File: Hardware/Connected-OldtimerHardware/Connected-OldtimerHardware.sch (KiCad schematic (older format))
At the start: 16 parts, among them J1 CAN_Bus_Connector, J2 MainConnector, J3 NextionConnector, Q1 2N3906, U1 ParticleElectron, U2 TSR_2-2450, U3 CANTranceiverModule, U4 AdafruitFRAM, U5 AdafruitUltimateGPS, U6 MotionSensor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

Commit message: reordered can module pins
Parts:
- U3: footprint (none) -> heathsfootprints:CAN_Tranceiver_Module
- U4: footprint (none) -> heathsfootprints:Adafruit_I2C_FRAM
- U5: footprint (none) -> heathsfootprints:AdafruitUltimateGPS
- U6: footprint (none) -> heathsfootprints:ShockSensor
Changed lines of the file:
@@
 F 0 "U3" H 4977 1446 50  0000 L CNN
 F 1 "CANTranceiverModule" H 4977 1355 50  0000 L CNN
-F 2 "" H 4950 1300 50  0001 C CNN
+F 2 "heathsfootprints:CAN_Tranceiver_Module" H 4950 1300 50  0001 C CNN
 F 3 "" H 4950 1300 50  0001 C CNN
 	1    4950 1300
@@
 F 0 "U4" H 5078 2746 50  0000 L CNN
 F 1 "AdafruitFRAM" H 5078 2655 50  0000 L CNN
-F 2 "" H 4600 2800 50  0001 C CNN
+F 2 "heathsfootprints:Adafruit_I2C_FRAM" H 4600 2800 50  0001 C CNN
 F 3 "" H 4600 2800 50  0001 C CNN
 	1    4600 2800
@@
 F 0 "U5" H 5127 4771 50  0000 L CNN
 F 1 "AdafruitUltimateGPS" H 5127 4680 50  0000 L CNN
-F 2 "" H 4750 4700 50  0001 C CNN
+F 2 "heathsfootprints:AdafruitUltimateGPS" H 4750 4700 50  0001 C CNN
 F 3 "" H 4750 4700 50  0001 C CNN
 	1    4750 4700
@@
 F 0 "U6" H 7377 3246 50  0000 L CNN
 F 1 "MotionSensor" H 7377 3155 50  0000 L CNN
-F 2 "" H 7300 3200 50  0001 C CNN
+F 2 "heathsfootprints:ShockSensor" H 7300 3200 50  0001 C CNN
 F 3 "" H 7300 3200 50  0001 C CNN
 	1    7300 3200

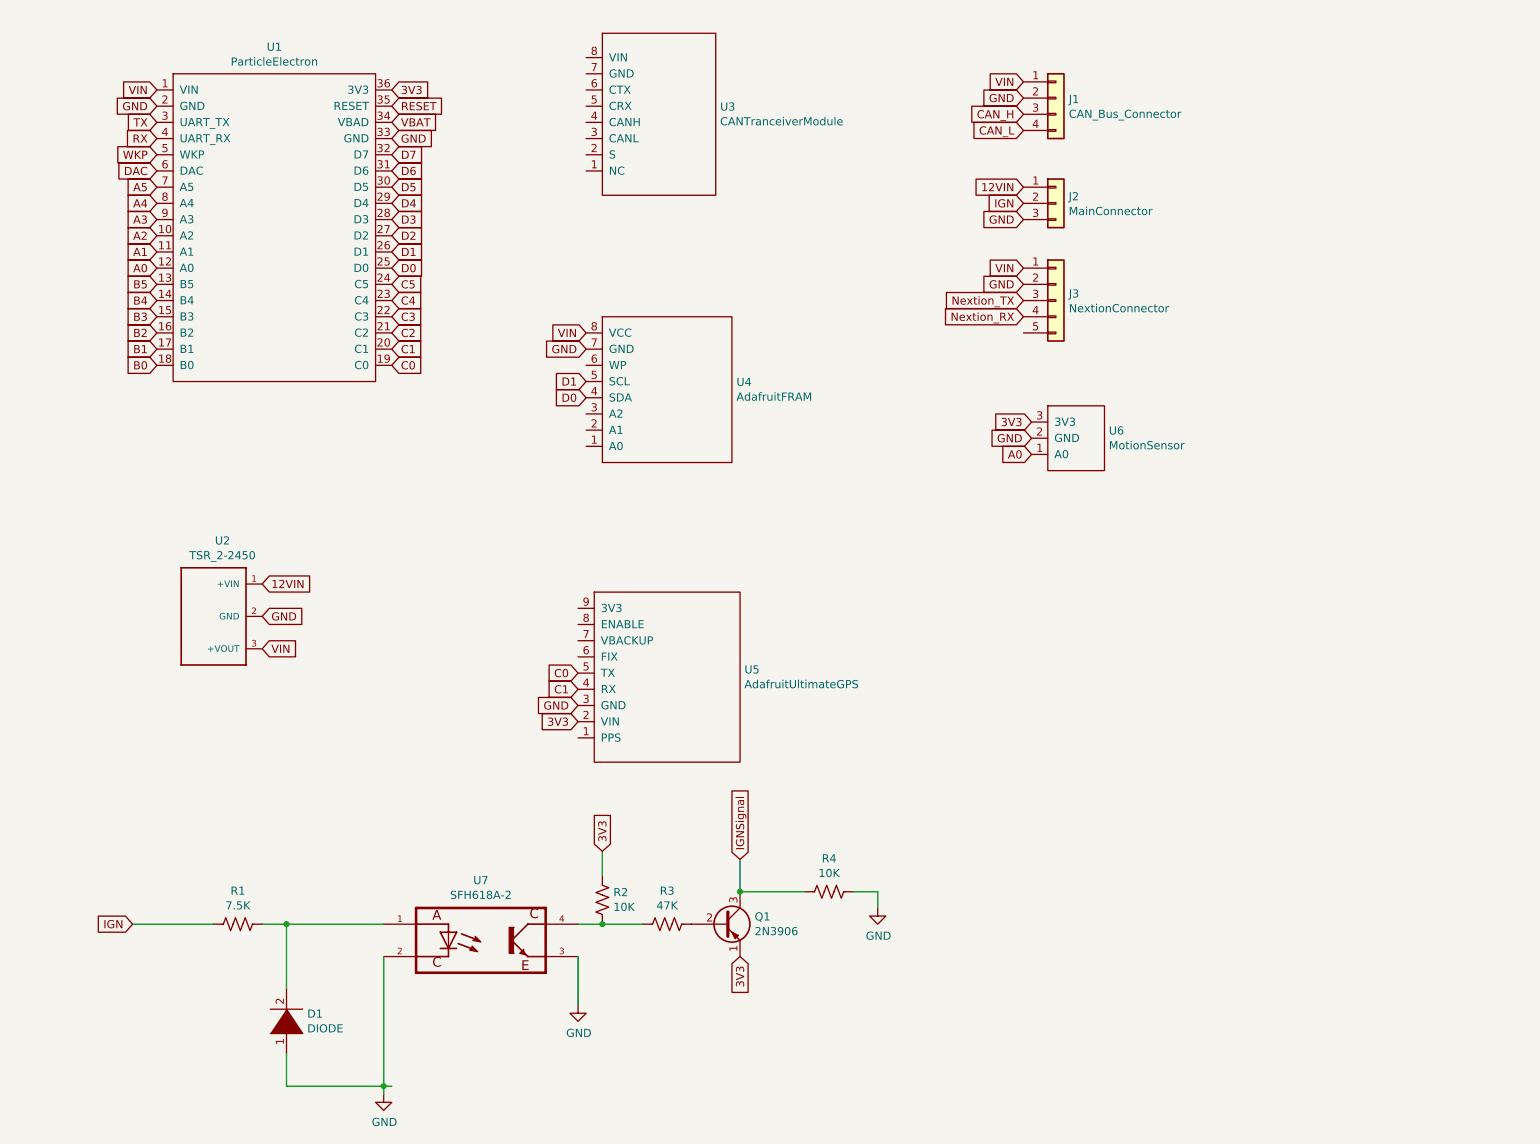
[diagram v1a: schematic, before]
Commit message: renamed pinflags to purposes
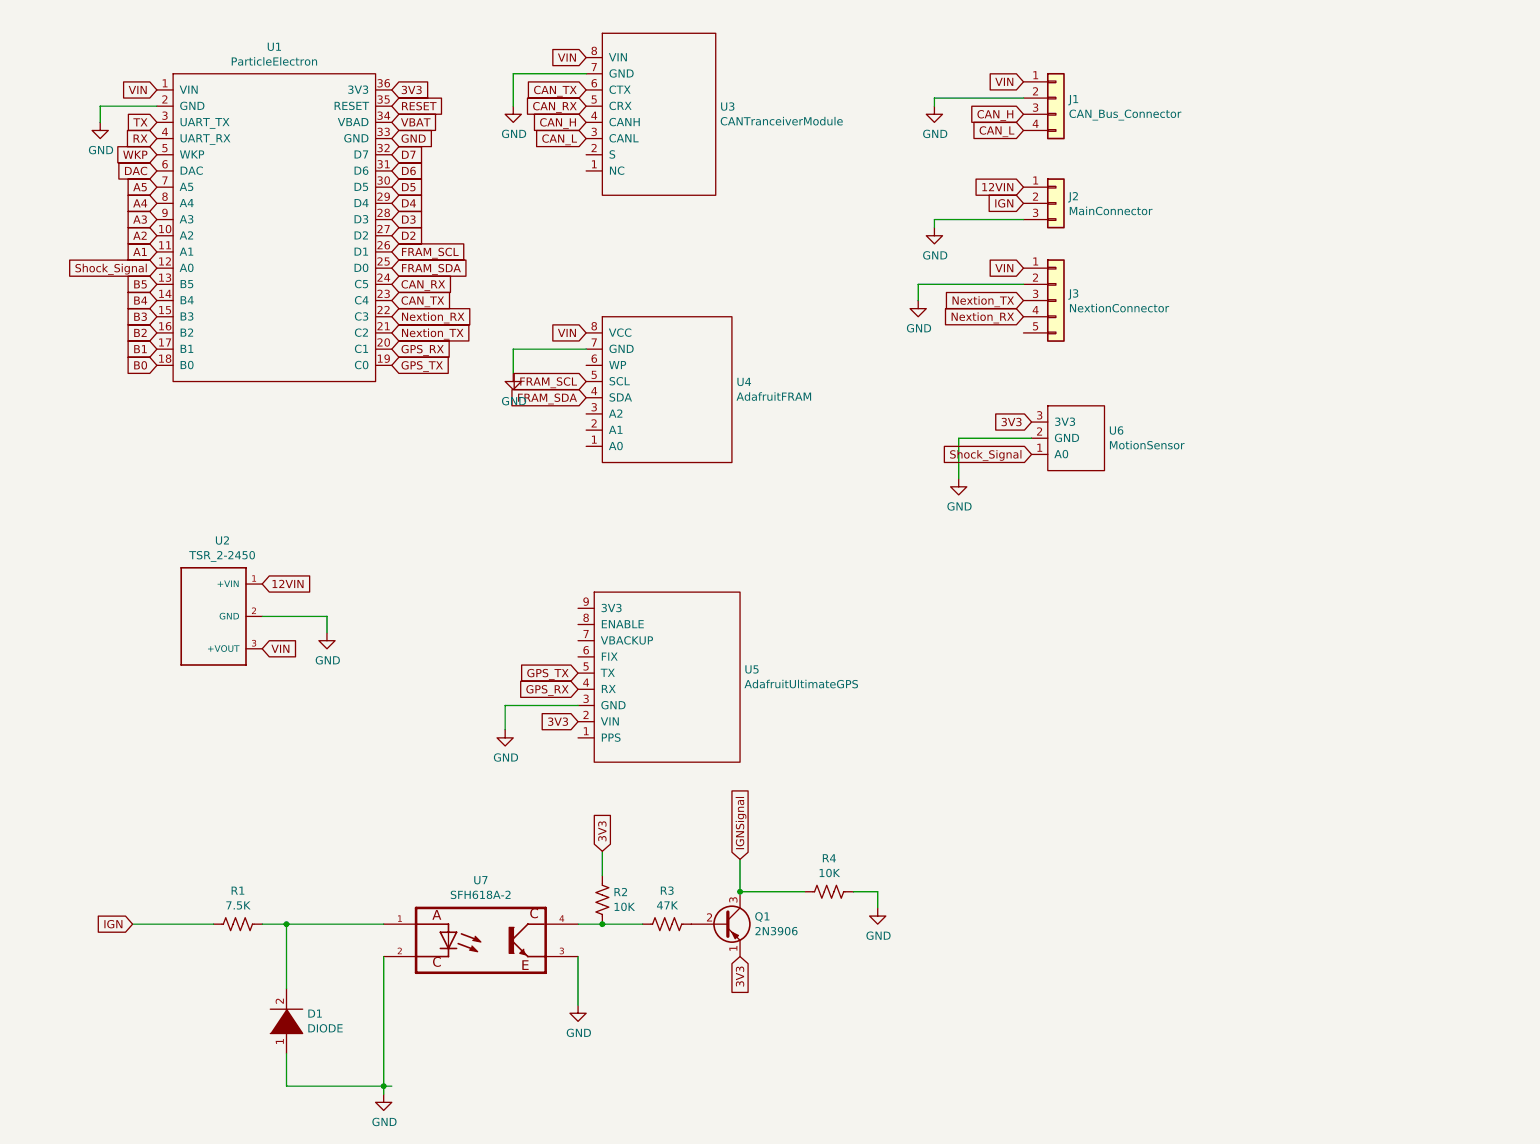
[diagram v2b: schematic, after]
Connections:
- net labels added: CAN_RX, CAN_TX, FRAM_SCL, FRAM_SDA, GPS_RX, GPS_TX, Shock_Signal
- net labels removed: A0, C0, C1, C2, C3, C4, C5, D0, D1
- wire segments 17 -> 35
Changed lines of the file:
@@
 Text GLabel 1500 1050 0    50   Input ~ 0
 VIN
-Text GLabel 1500 1150 0    50   Input ~ 0
-GND
 Text GLabel 1500 1250 0    50   Input ~ 0
 TX
@@
 A1
 Text GLabel 1500 2150 0    50   Input ~ 0
-A0
+Shock_Signal
 Text GLabel 1500 2250 0    50   Input ~ 0
 B5
@@
 Text GLabel 4150 2550 0    50   Input ~ 0
 VIN
-Text GLabel 4150 2650 0    50   Input ~ 0
-GND
 Text GLabel 4150 2850 0    50   Input ~ 0
-D1
+FRAM_SCL
 Text GLabel 4150 2950 0    50   Input ~ 0
-D0
+FRAM_SDA
 Text GLabel 4100 4950 0    50   Input ~ 0
 3V3
-Text GLabel 4100 4850 0    50   Input ~ 0
-GND
 Text GLabel 4100 4750 0    50   Input ~ 0
-C1
+GPS_RX
 Text GLabel 4100 4650 0    50   Input ~ 0
-C0
+GPS_TX
 $Comp
 L Connector_Generic:Conn_01x04 J1
@@
 Text GLabel 6850 1000 0    50   Input ~ 0
 VIN
-Text GLabel 6850 1100 0    50   Input ~ 0
-GND
 Text GLabel 6850 1200 0    50   Input ~ 0
 CAN_H
@@
 Text GLabel 6900 3100 0    50   Input ~ 0
 3V3
-Text GLabel 6900 3200 0    50   Input ~ 0
-GND
 Text GLabel 6900 3300 0    50   Input ~ 0
-A0
+Shock_Signal
 $Comp
 L Connected-OldtimerHardware-rescue:CANTranceiverModule-HeathsComponents U3
@@
 D2
 Text GLabel 2950 2050 2    50   Input ~ 0
-D1
+FRAM_SCL
 Text GLabel 2950 2150 2    50   Input ~ 0
-D0
-Text GLabel 2950 2250 2    50   Input ~ 0
-C5
-Text GLabel 2950 2350 2    50   Input ~ 0
-C4
+FRAM_SDA
 Text GLabel 2950 2450 2    50   Input ~ 0
-C3
+Nextion_RX
 Text GLabel 2950 2550 2    50   Input ~ 0
-C2
+Nextion_TX
 Text GLabel 2950 2650 2    50   Input ~ 0
-C1
+GPS_RX
 Text GLabel 2950 2750 2    50   Input ~ 0
-C0
+GPS_TX
 $Comp
 L Connected-OldtimerHardware-rescue:AdafruitFRAM-HeathsComponents U4
@@
 Text GLabel 2150 4100 2    50   Input ~ 0
 12VIN
-Text GLabel 2150 4300 2    50   Input ~ 0
-GND
 Text GLabel 2150 4500 2    50   Input ~ 0
 VIN
@@
 Text GLabel 6850 1750 0    50   Input ~ 0
 IGN
-Text GLabel 6850 1850 0    50   Input ~ 0
-GND
 Text GLabel 6850 2150 0    50   Input ~ 0
 VIN
-Text GLabel 6850 2250 0    50   Input ~ 0
-GND
 Text GLabel 6850 2350 0    50   Input ~ 0
 Nextion_TX
@@
 	1    0    0    -1
 $EndComp
+Text GLabel 4150 850  0    50   Input ~ 0
+VIN
+$Comp
+L power:GND #PWR?
+U 1 1 5D6E3912
+P 3700 1150
+F 0 "#PWR?" H 3700 900 50  0001 C CNN
+F 1 "GND" H 3705 977 50  0000 C CNN
+F 2 "" H 3700 1150 50  0001 C CNN
+F 3 "" H 3700 1150 50  0001 C CNN
+	1    3700 1150
+	1    0    0    -1
+$EndComp
+Wire Wire Line
+	4150 950  3700 950
+Wire Wire Line
+	3700 950  3700 1150
+Text GLabel 4150 1250 0    50   Input ~ 0
+CAN_H
+Text GLabel 4150 1350 0    50   Input ~ 0
+CAN_L
+Text GLabel 4150 1050 0    50   Input ~ 0
+CAN_TX
+Text GLabel 4150 1150 0    50   Input ~ 0
+CAN_RX
+Text GLabel 2950 2350 2    50   Input ~ 0
+CAN_TX
+Text GLabel 2950 2250 2    50   Input ~ 0
+CAN_RX
+$Comp
+L power:GND #PWR?
+U 1 1 5D6E4235
+P 3700 2800
+F 0 "#PWR?" H 3700 2550 50  0001 C CNN
+F 1 "GND" H 3705 2627 50  0000 C CNN
+F 2 "" H 3700 2800 50  0001 C CNN
+F 3 "" H 3700 2800 50  0001 C CNN
+	1    3700 2800
+	1    0    0    -1
+$EndComp
+Wire Wire Line
+	4150 2650 3700 2650
+Wire Wire Line
+	3700 2650 3700 2800
+$Comp
+L power:GND #PWR?
+U 1 1 5D6E45EA
+P 3650 5000
+F 0 "#PWR?" H 3650 4750 50  0001 C CNN
+F 1 "GND" H 3655 4827 50  0000 C CNN
+F 2 "" H 3650 5000 50  0001 C CNN
+F 3 "" H 3650 5000 50  0001 C CNN
+	1    3650 5000
+	1    0    0    -1
+$EndComp
+Wire Wire Line
+	4100 4850 3650 4850
+Wire Wire Line
+	3650 4850 3650 5000
+$Comp
+L power:GND #PWR?
+U 1 1 5D6E50E1
+P 6300 1150
+F 0 "#PWR?" H 6300 900 50  0001 C CNN
+F 1 "GND" H 6305 977 50  0000 C CNN
+F 2 "" H 6300 1150 50  0001 C CNN
+F 3 "" H 6300 1150 50  0001 C CNN
+	1    6300 1150
+	1    0    0    -1
+$EndComp
+$Comp
+L power:GND #PWR?
+U 1 1 5D6E5123
+P 6200 2350
+F 0 "#PWR?" H 6200 2100 50  0001 C CNN
+F 1 "GND" H 6205 2177 50  0000 C CNN
+F 2 "" H 6200 2350 50  0001 C CNN
+F 3 "" H 6200 2350 50  0001 C CNN
+	1    6200 2350
+	1    0    0    -1
+$EndComp
+$Comp
+L power:GND #PWR?
+U 1 1 5D6E51A5
+P 6450 3450
+F 0 "#PWR?" H 6450 3200 50  0001 C CNN
+F 1 "GND" H 6455 3277 50  0000 C CNN
+F 2 "" H 6450 3450 50  0001 C CNN
+F 3 "" H 6450 3450 50  0001 C CNN
+	1    6450 3450
+	1    0    0    -1
+$EndComp
+Wire Wire Line
+	6900 3200 6450 3200
+Wire Wire Line
+	6450 3200 6450 3450
+Wire Wire Line
+	6850 2250 6200 2250
+Wire Wire Line
+	6200 2250 6200 2350
+Wire Wire Line
+	6850 1100 6300 1100
+Wire Wire Line
+	6300 1100 6300 1150
+$Comp
+L power:GND #PWR?
+U 1 1 5D6E5CD7
+P 6300 1900
+F 0 "#PWR?" H 6300 1650 50  0001 C CNN
+F 1 "GND" H 6305 1727 50  0000 C CNN
+F 2 "" H 6300 1900 50  0001 C CNN
+F 3 "" H 6300 1900 50  0001 C CNN
+	1    6300 1900
+	1    0    0    -1
+$EndComp
+Wire Wire Line
+	6850 1850 6300 1850
+Wire Wire Line
+	6300 1850 6300 1900
+$Comp
+L power:GND #PWR?
+U 1 1 5D6E6529
+P 2550 4400
+F 0 "#PWR?" H 2550 4150 50  0001 C CNN
+F 1 "GND" H 2555 4227 50  0000 C CNN
+F 2 "" H 2550 4400 50  0001 C CNN
+F 3 "" H 2550 4400 50  0001 C CNN
+	1    2550 4400
+	1    0    0    -1
+$EndComp
+Wire Wire Line
+	2150 4300 2550 4300
+Wire Wire Line
+	2550 4300 2550 4400
+$Comp
+L power:GND #PWR?
+U 1 1 5D6E6E4F
+P 1150 1250
+F 0 "#PWR?" H 1150 1000 50  0001 C CNN
+F 1 "GND" H 1155 1077 50  0000 C CNN
+F 2 "" H 1150 1250 50  0001 C CNN
+F 3 "" H 1150 1250 50  0001 C CNN
+	1    1150 1250
+	1    0    0    -1
+$EndComp
+Wire Wire Line
+	1500 1150 1150 1150
+Wire Wire Line
+	1150 1150 1150 1250
 $EndSCHEMATC
